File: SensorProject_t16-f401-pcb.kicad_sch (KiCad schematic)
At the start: 56 parts, among them J1 Conn_01x02_Pin, J10 Conn_01x02_Pin, J11 Conn_01x02_Pin, J12 Conn_01x02_Pin, J13 Conn_01x02_Pin, J14 Conn_01x02_Pin, J15 Conn_01x02_Pin, J16 Conn_01x02_Pin, J17 Conn_01x04_Pin, J18 PinSocket_1x20_P2.54mm_Vertic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, J19 PinSocket_1x20_P2.54mm_Vertic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, J2 Conn_01x02_Pin, J20 Screw_Terminal_01x02, J3 Conn_01x02_Pin, J4 Conn_01x02_Pin, J5 Conn_01x02_Pin, J6 Conn_01x02_Pin, J7 Conn_01x02_Pin, J8 Conn_01x02_Pin, J9 Conn_01x02_Pin, U1 ADS1115IDGS, U2 ADS1115IDGS, U3 ADS1115IDGS, U4 ADS1115IDGS

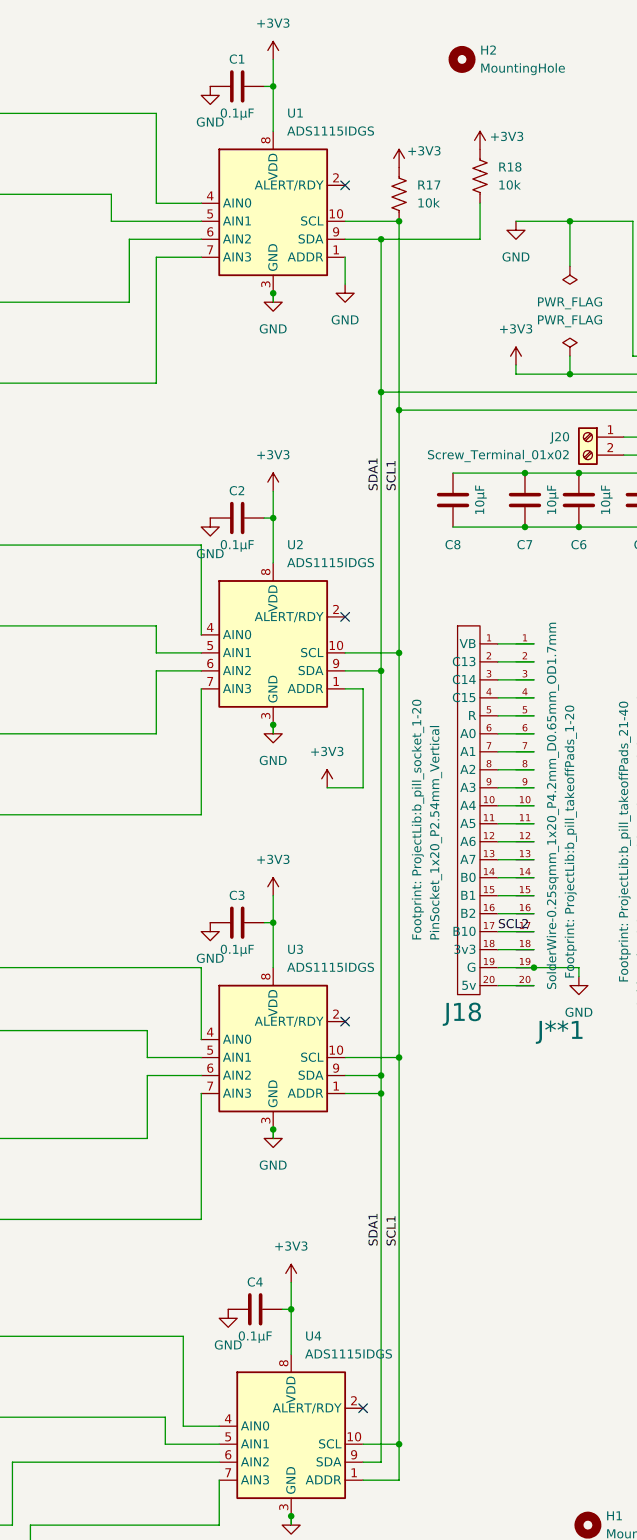
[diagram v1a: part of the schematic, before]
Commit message: added 10k pullups on ads alert/rdy pins.
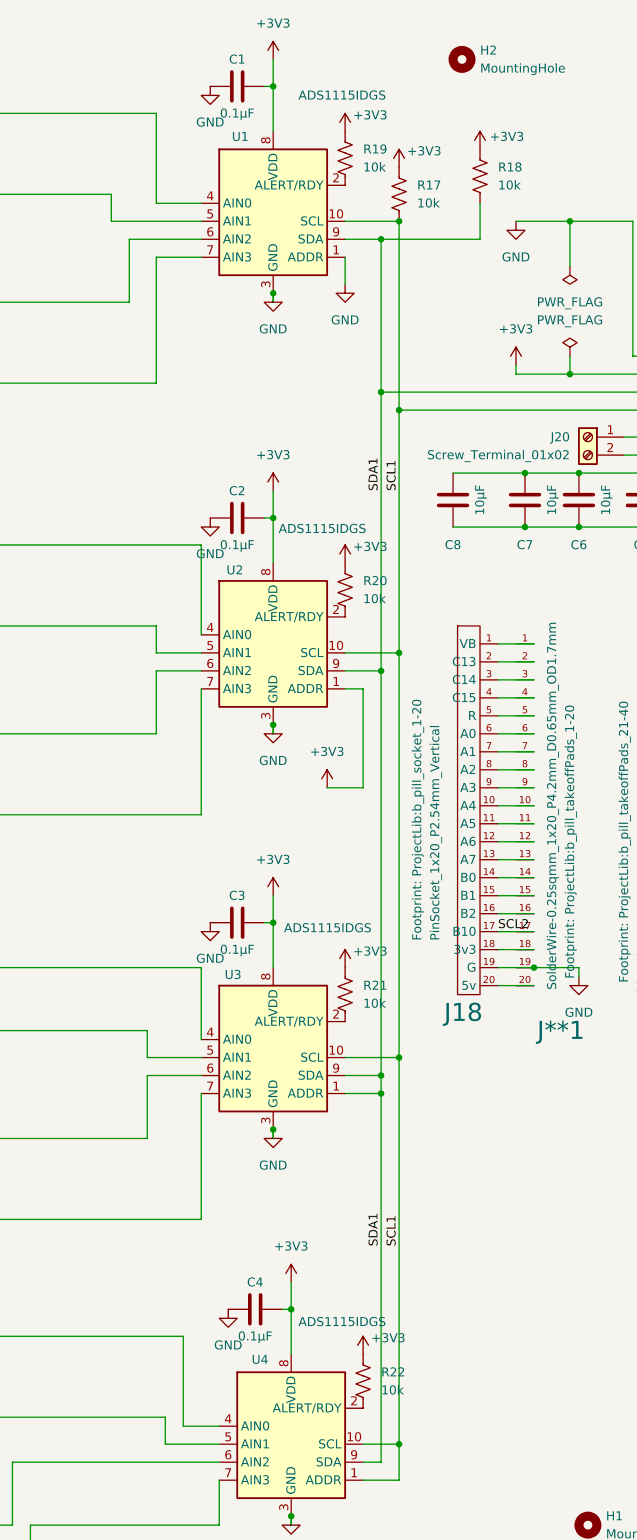
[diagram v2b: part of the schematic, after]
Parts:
- added R19, R20, R21, R22: 10k, ProjectLib:R_0603_1608Metric, symbol ProjectLib:R_US
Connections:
- net +3V3: now also R19.1, R20.1, R21.1, R22.1
- net at U1.2 (ALERT/RDY): now also R19.2
- net at U4.2 (ALERT/RDY): now also R22.2
- net at U3.2 (ALERT/RDY): now also R21.2
- net at U2.2 (ALERT/RDY): now also R20.2
- no-connect marks 4 -> 0
